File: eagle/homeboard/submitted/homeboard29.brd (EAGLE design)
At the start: 94 x 71.8 mm, 126 parts, among them IC1 XCF02S, IC2 25LC080SN, IC3 ATMEGA32U2-TQFP, Q5 BC848SMD, Q6 BC848SMD, Q7 BC848SMD, Q8 BC848SMD, T1 BSS138, T2 BC848, T3 BSS138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

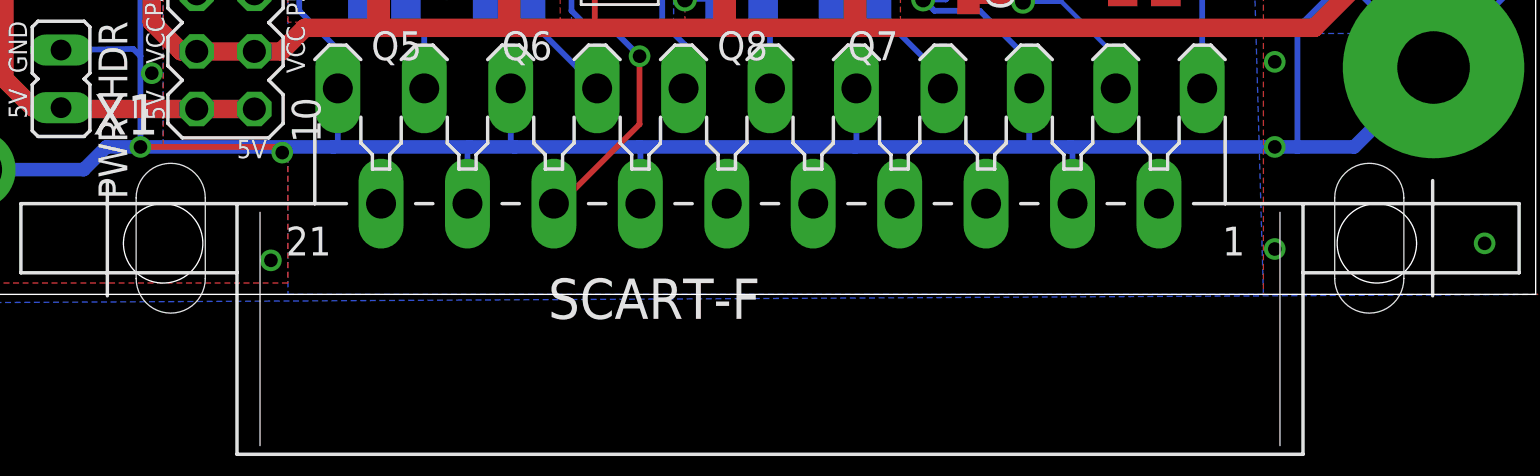
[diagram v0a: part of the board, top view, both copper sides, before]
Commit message: reverted changes to submitted homeboard29, moved recent changes to 29 into 30 and re-applied scart slot fix
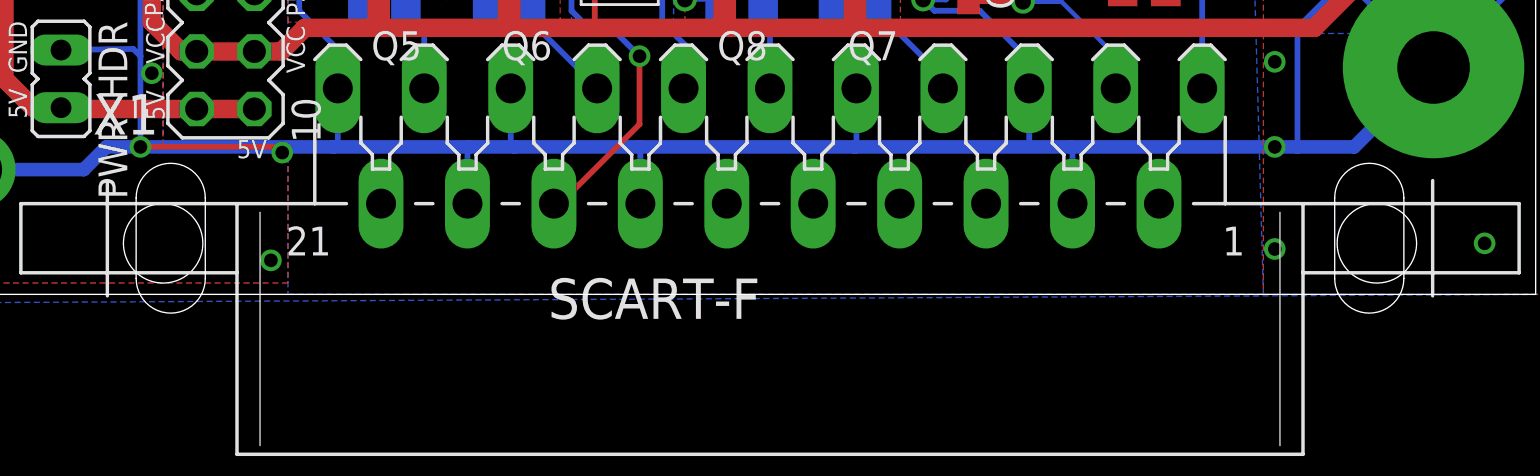
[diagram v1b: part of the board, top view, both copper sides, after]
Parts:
- C1, C3, C4, C5: value 100nF -> (none)
- C37, C38: value 20pF -> (none)
- LED1: value 20mA -> (none)
- R11, R23, R34: value 75 -> (none)
- R48, R49: value 2200 -> (none)
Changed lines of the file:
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@@
 <layers>
 <layer number="1" name="Top" color="4" fill="1" visible="yes" active="yes"/>
-<layer number="16" name="Bottom" color="1" fill="1" visible="no" active="yes"/>
+<layer number="16" name="Bottom" color="1" fill="1" visible="yes" active="yes"/>
 <layer number="17" name="Pads" color="2" fill="1" visible="yes" active="yes"/>
 <layer number="18" name="Vias" color="2" fill="1" visible="yes" active="yes"/>
@@
 <layer number="20" name="Dimension" color="15" fill="1" visible="yes" active="yes"/>
 <layer number="21" name="tPlace" color="7" fill="1" visible="yes" active="yes"/>
-<layer number="22" name="bPlace" color="7" fill="1" visible="no" active="yes"/>
+<layer number="22" name="bPlace" color="7" fill="1" visible="yes" active="yes"/>
 <layer number="23" name="tOrigins" color="15" fill="1" visible="yes" active="yes"/>
-<layer number="24" name="bOrigins" color="15" fill="1" visible="no" active="yes"/>
+<layer number="24" name="bOrigins" color="15" fill="1" visible="yes" active="yes"/>
 <layer number="25" name="tNames" color="7" fill="1" visible="yes" active="yes"/>
-<layer number="26" name="bNames" color="7" fill="1" visible="no" active="yes"/>
+<layer number="26" name="bNames" color="7" fill="1" visible="yes" active="yes"/>
 <layer number="27" name="tValues" color="7" fill="1" visible="no" active="yes"/>
 <layer number="28" name="bValues" color="7" fill="1" visible="no" active="yes"/>
@@
 <layer number="32" name="bCream" color="7" fill="5" visible="no" active="yes"/>
 <layer number="33" name="tFinish" color="6" fill="3" visible="yes" active="yes"/>
-<layer number="34" name="bFinish" color="6" fill="6" visible="no" active="yes"/>
+<layer number="34" name="bFinish" color="6" fill="6" visible="yes" active="yes"/>
 <layer number="35" name="tGlue" color="7" fill="4" visible="no" active="yes"/>
 <layer number="36" name="bGlue" color="7" fill="5" visible="no" active="yes"/>
@@
 <layer number="38" name="bTest" color="7" fill="1" visible="no" active="yes"/>
 <layer number="39" name="tKeepout" color="4" fill="11" visible="yes" active="yes"/>
-<layer number="40" name="bKeepout" color="1" fill="11" visible="no" active="yes"/>
+<layer number="40" name="bKeepout" color="1" fill="11" visible="yes" active="yes"/>
 <layer number="41" name="tRestrict" color="4" fill="10" visible="yes" active="yes"/>
-<layer number="42" name="bRestrict" color="1" fill="10" visible="no" active="yes"/>
+<layer number="42" name="bRestrict" color="1" fill="10" visible="yes" active="yes"/>
 <layer number="43" name="vRestrict" color="2" fill="10" visible="no" active="yes"/>
-<layer number="44" name="Drills" color="7" fill="1" visible="no" active="yes"/>
-<layer number="45" name="Holes" color="7" fill="1" visible="no" active="yes"/>
+<layer number="44" name="Drills" color="7" fill="1" visible="yes" active="yes"/>
+<layer number="45" name="Holes" color="7" fill="1" visible="yes" active="yes"/>
 <layer number="46" name="Milling" color="3" fill="1" visible="no" active="yes"/>
 <layer number="47" name="Measures" color="7" fill="1" visible="no" active="yes"/>
@@
 <element name="Q7" library="bc548" package="SOT23" value="BC848SMD" x="64" y="13.5" rot="R180"/>
 <element name="Q8" library="bc548" package="SOT23" value="BC848SMD" x="58.25" y="13.5" rot="R180"/>
-<element name="R23" library="resistor" package="M0805" value="75" x="66.75" y="19" rot="R270"/>
-<element name="R34" library="resistor" package="M0805" value="75" x="71.25" y="16" rot="R270"/>
-<element name="C3" library="resistor" package="C0603" value="100nF" x="69" y="13.75" rot="R270"/>
-<element name="C4" library="resistor" package="C0603" value="100nF" x="80.5" y="13.5"/>
+<element name="R23" library="resistor" package="M0805" value="" x="66.75" y="19" rot="R270"/>
+<element name="R34" library="resistor" package="M0805" value="" x="71.25" y="16" rot="R270"/>
+<element name="C3" library="resistor" package="C0603" value="" x="69" y="13.75" rot="R270"/>
+<element name="C4" library="resistor" package="C0603" value="" x="80.5" y="13.5"/>
 <element name="U$2" library="cpcfpga" package="OSC_7C" value="TXO_7C" x="53.625" y="15.375" rot="R90"/>
 <element name="REG2.5" library="cpcfpga" package="SOT223" value="2.5V" x="9.5" y="43.25" rot="R270"/>
@@
 <attribute name="OC_FARNELL" value="1137302" x="69.280334375" y="39.08058125" size="1.778" layer="27" display="off"/>
 </element>
-<element name="R48" library="resistor" package="M0805" value="2200" x="69" y="17.5" rot="R270"/>
-<element name="C1" library="resistor" package="C0603" value="100nF" x="66.75" y="15.25" rot="R90"/>
-<element name="C5" library="resistor" package="C0603" value="100nF" x="73.5" y="14.75" rot="R270"/>
-<element name="R49" library="resistor" package="M0805" value="2200" x="76.75" y="13.5"/>
+<element name="R48" library="resistor" package="M0805" value="" x="69" y="17.5" rot="R270"/>
+<element name="C1" library="resistor" package="C0603" value="" x="66.75" y="15.25" rot="R90"/>
+<element name="C5" library="resistor" package="C0603" value="" x="73.5" y="14.75" rot="R270"/>
+<element name="R49" library="resistor" package="M0805" value="" x="76.75" y="13.5"/>
 <element name="R50" library="resistor" package="M0805" value="2k2" x="40.75" y="18.25" rot="MR90"/>
 <element name="IC3" library="adafruit" package="TQFP32-08" value="ATMEGA32U2-TQFP" x="77.46966875" y="38.823221875"/>
@@
 </element>
 <element name="Q1" library="special" package="QS" value="" x="72.75" y="54.25"/>
-<element name="C37" library="rcl" package="C0805" value="20pF" x="71.5" y="50.5" rot="R180"/>
-<element name="C38" library="rcl" package="C0805" value="20pF" x="76.5" y="50.5"/>
+<element name="C37" library="rcl" package="C0805" value="" x="71.5" y="50.5" rot="R180"/>
+<element name="C38" library="rcl" package="C0805" value="" x="76.5" y="50.5"/>
 <element name="PWR_HDR" library="jumper" package="JP1" value="" x="29" y="9.5" rot="R180"/>
 <element name="X8" library="cpcfpga" package="20-0137" value="STEREOJACK" x="6.75" y="63.25" rot="R270"/>
@@
 <attribute name="OC_FARNELL" value="unknown" x="90.5" y="30" size="1.778" layer="27" rot="R270" display="off"/>
 </element>
-<element name="R11" library="resistor" package="M0805" value="75" x="81" y="52.5" rot="R90"/>
-<element name="LED1" library="adafruit" package="CHIPLED_0805" value="20mA" x="84" y="53.5" rot="R270"/>
+<element name="R11" library="resistor" package="M0805" value="" x="81" y="52.5" rot="R90"/>
+<element name="LED1" library="adafruit" package="CHIPLED_0805" value="" x="84" y="53.5" rot="R270"/>
 </elements>
 <signals>

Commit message: added some more notes to homeboard
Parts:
- C1, C3, C4, C5: value (none) -> 100nF
- R23, R34: value (none) -> 75
- R48, R49: value (none) -> 2200
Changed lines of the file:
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@@
 <layers>
 <layer number="1" name="Top" color="4" fill="1" visible="yes" active="yes"/>
-<layer number="16" name="Bottom" color="1" fill="1" visible="yes" active="yes"/>
+<layer number="16" name="Bottom" color="1" fill="1" visible="no" active="yes"/>
 <layer number="17" name="Pads" color="2" fill="1" visible="yes" active="yes"/>
 <layer number="18" name="Vias" color="2" fill="1" visible="yes" active="yes"/>
@@
 <layer number="20" name="Dimension" color="15" fill="1" visible="yes" active="yes"/>
 <layer number="21" name="tPlace" color="7" fill="1" visible="yes" active="yes"/>
-<layer number="22" name="bPlace" color="7" fill="1" visible="yes" active="yes"/>
+<layer number="22" name="bPlace" color="7" fill="1" visible="no" active="yes"/>
 <layer number="23" name="tOrigins" color="15" fill="1" visible="yes" active="yes"/>
-<layer number="24" name="bOrigins" color="15" fill="1" visible="yes" active="yes"/>
+<layer number="24" name="bOrigins" color="15" fill="1" visible="no" active="yes"/>
 <layer number="25" name="tNames" color="7" fill="1" visible="yes" active="yes"/>
-<layer number="26" name="bNames" color="7" fill="1" visible="yes" active="yes"/>
+<layer number="26" name="bNames" color="7" fill="1" visible="no" active="yes"/>
 <layer number="27" name="tValues" color="7" fill="1" visible="no" active="yes"/>
 <layer number="28" name="bValues" color="7" fill="1" visible="no" active="yes"/>
@@
 <layer number="32" name="bCream" color="7" fill="5" visible="no" active="yes"/>
 <layer number="33" name="tFinish" color="6" fill="3" visible="yes" active="yes"/>
-<layer number="34" name="bFinish" color="6" fill="6" visible="yes" active="yes"/>
+<layer number="34" name="bFinish" color="6" fill="6" visible="no" active="yes"/>
 <layer number="35" name="tGlue" color="7" fill="4" visible="no" active="yes"/>
 <layer number="36" name="bGlue" color="7" fill="5" visible="no" active="yes"/>
@@
 <layer number="38" name="bTest" color="7" fill="1" visible="no" active="yes"/>
 <layer number="39" name="tKeepout" color="4" fill="11" visible="yes" active="yes"/>
-<layer number="40" name="bKeepout" color="1" fill="11" visible="yes" active="yes"/>
+<layer number="40" name="bKeepout" color="1" fill="11" visible="no" active="yes"/>
 <layer number="41" name="tRestrict" color="4" fill="10" visible="yes" active="yes"/>
-<layer number="42" name="bRestrict" color="1" fill="10" visible="yes" active="yes"/>
+<layer number="42" name="bRestrict" color="1" fill="10" visible="no" active="yes"/>
 <layer number="43" name="vRestrict" color="2" fill="10" visible="no" active="yes"/>
-<layer number="44" name="Drills" color="7" fill="1" visible="yes" active="yes"/>
-<layer number="45" name="Holes" color="7" fill="1" visible="yes" active="yes"/>
+<layer number="44" name="Drills" color="7" fill="1" visible="no" active="yes"/>
+<layer number="45" name="Holes" color="7" fill="1" visible="no" active="yes"/>
 <layer number="46" name="Milling" color="3" fill="1" visible="no" active="yes"/>
 <layer number="47" name="Measures" color="7" fill="1" visible="no" active="yes"/>
@@
 <element name="Q7" library="bc548" package="SOT23" value="BC848SMD" x="64" y="13.5" rot="R180"/>
 <element name="Q8" library="bc548" package="SOT23" value="BC848SMD" x="58.25" y="13.5" rot="R180"/>
-<element name="R23" library="resistor" package="M0805" value="" x="66.75" y="19" rot="R270"/>
-<element name="R34" library="resistor" package="M0805" value="" x="71.25" y="16" rot="R270"/>
-<element name="C3" library="resistor" package="C0603" value="" x="69" y="13.75" rot="R270"/>
-<element name="C4" library="resistor" package="C0603" value="" x="80.5" y="13.5"/>
+<element name="R23" library="resistor" package="M0805" value="75" x="66.75" y="19" rot="R270"/>
+<element name="R34" library="resistor" package="M0805" value="75" x="71.25" y="16" rot="R270"/>
+<element name="C3" library="resistor" package="C0603" value="100nF" x="69" y="13.75" rot="R270"/>
+<element name="C4" library="resistor" package="C0603" value="100nF" x="80.5" y="13.5"/>
 <element name="U$2" library="cpcfpga" package="OSC_7C" value="TXO_7C" x="53.625" y="15.375" rot="R90"/>
 <element name="REG2.5" library="cpcfpga" package="SOT223" value="2.5V" x="9.5" y="43.25" rot="R270"/>
@@
 <attribute name="OC_FARNELL" value="1137302" x="69.280334375" y="39.08058125" size="1.778" layer="27" display="off"/>
 </element>
-<element name="R48" library="resistor" package="M0805" value="" x="69" y="17.5" rot="R270"/>
-<element name="C1" library="resistor" package="C0603" value="" x="66.75" y="15.25" rot="R90"/>
-<element name="C5" library="resistor" package="C0603" value="" x="73.5" y="14.75" rot="R270"/>
-<element name="R49" library="resistor" package="M0805" value="" x="76.75" y="13.5"/>
+<element name="R48" library="resistor" package="M0805" value="2200" x="69" y="17.5" rot="R270"/>
+<element name="C1" library="resistor" package="C0603" value="100nF" x="66.75" y="15.25" rot="R90"/>
+<element name="C5" library="resistor" package="C0603" value="100nF" x="73.5" y="14.75" rot="R270"/>
+<element name="R49" library="resistor" package="M0805" value="2200" x="76.75" y="13.5"/>
 <element name="R50" library="resistor" package="M0805" value="2k2" x="40.75" y="18.25" rot="MR90"/>
 <element name="IC3" library="adafruit" package="TQFP32-08" value="ATMEGA32U2-TQFP" x="77.46966875" y="38.823221875"/>

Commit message: added more values
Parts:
- C37, C38: value (none) -> 20pF
- LED1: value (none) -> 20mA
- R11: value (none) -> 75
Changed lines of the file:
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@@
 </element>
 <element name="Q1" library="special" package="QS" value="" x="72.75" y="54.25"/>
-<element name="C37" library="rcl" package="C0805" value="" x="71.5" y="50.5" rot="R180"/>
-<element name="C38" library="rcl" package="C0805" value="" x="76.5" y="50.5"/>
+<element name="C37" library="rcl" package="C0805" value="20pF" x="71.5" y="50.5" rot="R180"/>
+<element name="C38" library="rcl" package="C0805" value="20pF" x="76.5" y="50.5"/>
 <element name="PWR_HDR" library="jumper" package="JP1" value="" x="29" y="9.5" rot="R180"/>
 <element name="X8" library="cpcfpga" package="20-0137" value="STEREOJACK" x="6.75" y="63.25" rot="R270"/>
@@
 <attribute name="OC_FARNELL" value="unknown" x="90.5" y="30" size="1.778" layer="27" rot="R270" display="off"/>
 </element>
-<element name="R11" library="resistor" package="M0805" value="" x="81" y="52.5" rot="R90"/>
-<element name="LED1" library="adafruit" package="CHIPLED_0805" value="" x="84" y="53.5" rot="R270"/>
+<element name="R11" library="resistor" package="M0805" value="75" x="81" y="52.5" rot="R90"/>
+<element name="LED1" library="adafruit" package="CHIPLED_0805" value="20mA" x="84" y="53.5" rot="R270"/>
 </elements>
 <signals>
